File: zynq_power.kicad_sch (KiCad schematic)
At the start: 1 part, among them U2 XC7Z020-2CLG400I

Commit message: sch-updated
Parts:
- added C2, C200, C204, C209, C221, C224, C230, C233, C234, C235, C248: 100u, Capacitor_SMD:C_1206_3216Metric, symbol Device:C
- added C201, C205, C210, C216, C220, C223, C229, C232, C236, C237, C246, C247, C3: 4u7, Capacitor_SMD:C_0402_1005Metric, symbol Device:C
- added C202, C203, C206, C207, C208, C211, C215, C217, C218, C219, C222, C225, C226, C227, C228, C231, C238, C239, C240, C241, C242, C243, C244, C245, C4: 470n, Capacitor_SMD:C_0402_1005Metric, symbol Device:C
- added C400: 100n, Capacitor_SMD:C_0402_1005Metric, symbol Device:C
- added C612, C613: 47n, Capacitor_SMD:C_0402_1005Metric, symbol Device:C
- added FB200: 120R, FB_0402, symbol Schematic-Lib-PhilsLab:FB_0402
- added R401, R402: 12K, Resistor_SMD:R_0402_1005Metric, symbol Device:R
- added U1: XC7Z020-2CLG400I, Package_BGA:Xilinx_CLG400, symbol 2024-11-30_12-42-37:XC7Z020-2CLG400I
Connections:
- net GND: now reaches U2.F10 (RSVDGND)
- net GND: now also U2.A18 (GND), U2.B11 (GND), U2.C14 (GND), U2.C4 (GND), U2.C9 (GND), U2.D17 (GND), U2.E10 (GND), U2.E20 (GND), U2.F3 (GND), U2.F7 (GND), U2.G10 (GND), U2.G12 (GND), U2.G16 (GND), U2.H11 (GND), U2.H13 (GND), U2.H19 (GND), U2.H7 (GND), U2.H9 (GND), U2.J10 (GNDADC_0), U2.J12 (GND), U2.J2 (GND), U2.J8 (GND), U2.K11 (GND), U2.K13 (GND), U2.K15 (GND), U2.K5 (GND), U2.K7 (GND), U2.L12 (GND), U2.L18 (GND), U2.L8 (GND), U2.M1 (GND), U2.M11 (GND), U2.M13 (GND), U2.M7 (GND), U2.N10 (GND), U2.N12 (GND), U2.N14 (GND), U2.N4 (GND), U2.N8 (GND), U2.P11 (GND), U2.P13 (GND), U2.P17 (GND), U2.P7 (GND), U2.P9 (GND), U2.R12 (GND), U2.R8 (GND), U2.T3 (GND), U2.T7 (GND), U2.U6 (GND), U2.V9 (GND), U2.W2 (GND), U2.Y5 (GND), C2.2, C200.2, C201.2, C202.2, C203.2, C204.2, C205.2, C206.2, C207.2, C208.2, C209.2, C210.2, C211.2, C215.2, C216.2, C217.2, C218.2, C219.2, C220.2, C221.2, C222.2, C223.2, C224.2, C225.2, C226.2, C227.2, C228.2, C229.2, C230.2, C231.2, C232.2, C233.2, C234.2, C235.2, C236.2, C237.2, C238.2, C239.2, C240.2, C241.2, C242.2, C243.2, C244.2, C245.2, C246.2, C247.2, C248.2, C3.2, C4.2, C612.2, C613.2, U1.A8 (GND), U1.B1 (GND), U1.K10 (VREFN_0), U1.L9 (VREFP_0)
- net at U2.R20 (GND): now also U2.T13 (GND), U2.U16 (GND), U2.V19 (GND), U2.W12 (GND), U2.Y15 (GND)
- net at U2.E11 (PS_MIO_VREF_501): now also C400.1, R401.2, R402.1
- net +1V8: now reaches U2.F11 (VCCBATT_0)
- net +1V8: now also U2.J11 (VCCAUX), U2.J9 (VCCADC_0), U2.L11 (VCCAUX), U2.N11 (VCCAUX), U2.N9 (VCCAUX), U2.P10 (VCCAUX), U2.R9 (VCCAUX), C2.1, C217.1, C218.1, C219.1, C220.1, C221.1, C222.1, C223.1, C224.1, C3.1, C4.1, FB200.2, R402.2, U1.A13 (VCCO_MIO1_501), U1.B16 (VCCO_MIO1_501), U1.D12 (VCCO_MIO1_501), U1.E15 (VCCO_MIO1_501), U1.F8 (VCCPAUX), U1.G9 (VCCPAUX), U1.H8 (VCCPAUX), U1.K8 (VCCPAUX), U1.M8 (VCCPAUX)
- net PL_B35_L6_N: now reaches U2.F17 (IO_L6N_T0_VREF_35)
- net +1V0: now reaches U2.G11 (VCCBRAM)
- net +1V0: now also U2.G13 (VCCINT), U2.H10 (VCCBRAM), U2.H12 (VCCINT), U2.J13 (VCCINT), U2.K12 (VCCINT), U2.L13 (VCCINT), U2.M12 (VCCINT), U2.N13 (VCCINT), U2.P12 (VCCINT), U2.R13 (VCCINT), C200.1, C201.1, C202.1, C203.1, C204.1, C205.1, C206.1, C207.1, C208.1, C231.1, C232.1, C233.1, U1.G7 (VCCPINT), U1.J7 (VCCPINT), U1.L7 (VCCPINT), U1.N7 (VCCPINT), U1.P8 (VCCPINT), U1.R7 (VCCPINT)
- net +0V675: now reaches U2.H6 (PS_DDR_VREF0_502)
- net +0V675: now also U2.P6 (PS_DDR_VREF1_502), C612.1, C613.1
- net +3V3: now reaches U2.K6 (VCCO_0)
- net +3V3: now also U2.N6 (RSVDVCC3), U2.R6 (RSVDVCC2), U2.T6 (RSVDVCC1), C209.1, C210.1, C211.1, C234.1, C235.1, C236.1, C237.1, C238.1, C239.1, C240.1, C241.1, C242.1, C243.1, C244.1, C245.1, C246.1, C247.1, C248.1, U1.B6 (VCCO_MIO0_500), U1.C19 (VCCO_35), U1.D7 (VCCO_MIO0_500), U1.F18 (VCCO_35), U1.H14 (VCCO_35), U1.J17 (VCCO_35), U1.K20 (VCCO_35), U1.M16 (VCCO_35), U1.N19 (VCCO_34), U1.R15 (VCCO_34), U1.T18 (VCCO_34), U1.T8 (VCCO_13), U1.U11 (VCCO_13), U1.V14 (VCCO_34), U1.W17 (VCCO_34), U1.W7 (VCCO_13), U1.Y10 (VCCO_13), U1.Y20 (VCCO_34)
- new net: C400.2, R401.1
- new net +1V35: C225.1, C226.1, C227.1, C228.1, C229.1, C230.1, U1.A3 (VCCO_DDR_502), U1.D2 (VCCO_DDR_502), U1.E5 (VCCO_DDR_502), U1.G1 (VCCO_DDR_502), U1.H4 (VCCO_DDR_502), U1.L3 (VCCO_DDR_502), U1.P2 (VCCO_DDR_502), U1.R5 (VCCO_DDR_502), U1.U1 (VCCO_DDR_502), U1.V4 (VCCO_DDR_502)
- new net +1V8_PLL: C215.1, C216.1, FB200.1, U1.G8 (VCCPLL)
- no-connect marks 0 -> 4
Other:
- note added: "GND Connection"
- note added: "POWER & ETC"
- moved on the sheet: U2E, U2G, U2H

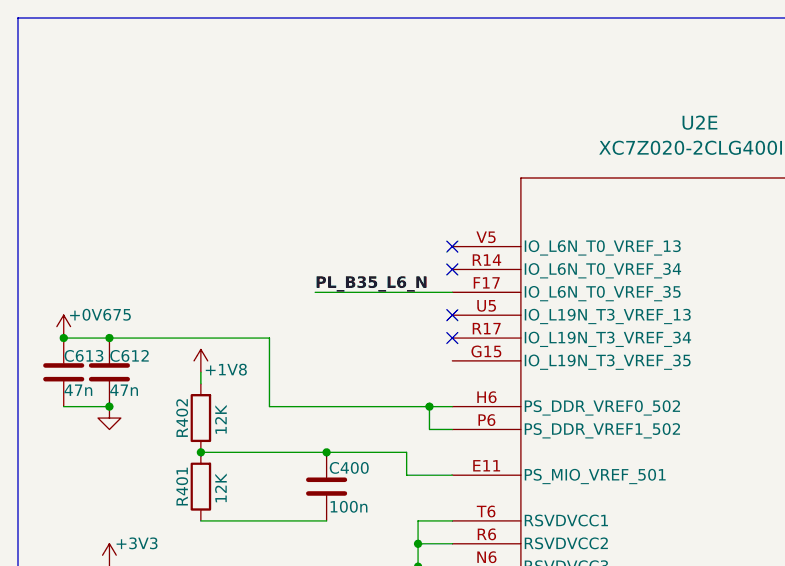
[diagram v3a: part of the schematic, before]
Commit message: sch updated zynq ddr
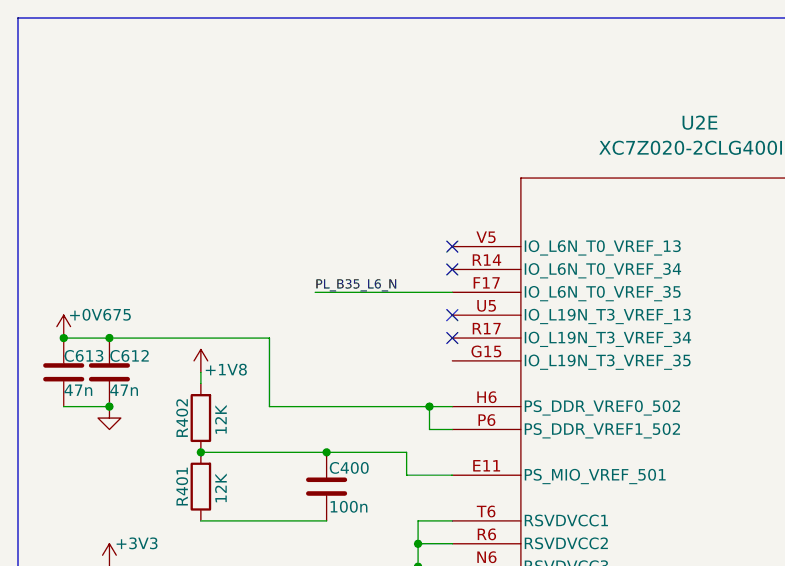
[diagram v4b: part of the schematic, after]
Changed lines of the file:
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@@
 		(effects
 			(font
-				(size 1.27 1.27)
-				(thickness 0.254)
-				(bold yes)
+				(size 1.016 1.016)
+				(thickness 0.127)
+				(color 82 86 255 1)
 			)
 			(justify left bottom)

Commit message: all page
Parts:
- removed C400: 100n, Capacitor_SMD:C_0402_1005Metric, symbol Device:C
- removed C612, C613: 47n, Capacitor_SMD:C_0402_1005Metric, symbol Device:C
- removed R401, R402: 12K, Resistor_SMD:R_0402_1005Metric, symbol Device:R
- removed U1, U2: XC7Z020-2CLG400I, Package_BGA:Xilinx_CLG400, symbol 2024-11-30_12-42-37:XC7Z020-2CLG400I
- added U6: XC7Z020-2CLG400I, zynq_sc7z0x0:CLG400, symbol Zynq_xc7z0x0-x:CMP-0363-00007-3
- renumbered C2 to C212, C3 to C213, C4 to C214
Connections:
- net +1V0: now also U6.G11 (VCCBRAM), U6.G13 (VCCINT), U6.G7 (VCCPINT), U6.H10 (VCCBRAM), U6.H12 (VCCINT), U6.J13 (VCCINT), U6.J7 (VCCPINT), U6.K12 (VCCINT), U6.L13 (VCCINT), U6.L7 (VCCPINT), U6.M12 (VCCINT), U6.N13 (VCCINT), U6.N7 (VCCPINT), U6.P12 (VCCINT), U6.P8 (VCCPINT), U6.R13 (VCCINT), U6.R7 (VCCPINT)
- net +1V35: now also U6.A3 (VCCO_DDR_502), U6.D2 (VCCO_DDR_502), U6.E5 (VCCO_DDR_502), U6.G1 (VCCO_DDR_502), U6.H4 (VCCO_DDR_502), U6.L3 (VCCO_DDR_502), U6.P2 (VCCO_DDR_502), U6.R5 (VCCO_DDR_502), U6.U1 (VCCO_DDR_502), U6.V4 (VCCO_DDR_502)
- net +1V8: now also U6.A13 (VCCO_MIO1_501), U6.B16 (VCCO_MIO1_501), U6.D12 (VCCO_MIO1_501), U6.E15 (VCCO_MIO1_501), U6.F11 (VCCBATT_0), U6.F8 (VCCPAUX), U6.G9 (VCCPAUX), U6.H8 (VCCPAUX), U6.J11 (VCCAUX), U6.J9 (VCCADC_0), U6.K8 (VCCPAUX), U6.L11 (VCCAUX), U6.M8 (VCCPAUX), U6.N11 (VCCAUX), U6.N9 (VCCAUX), U6.P10 (VCCAUX), U6.R9 (VCCAUX)
- net +1V8_PLL: now also U6.G8 (VCCPLL)
- net +3V3: now also U6.B6 (VCCO_MIO0_500), U6.C19 (VCCO_35), U6.D7 (VCCO_MIO0_500), U6.F18 (VCCO_35), U6.H14 (VCCO_35), U6.J17 (VCCO_35), U6.K20 (VCCO_35), U6.K6 (VCCO_0), U6.M16 (VCCO_35), U6.N19 (VCCO_34), U6.N6 (RSVDVCC3), U6.R15 (VCCO_34), U6.R6 (RSVDVCC2), U6.T18 (VCCO_34), U6.T6 (RSVDVCC1), U6.T8 (VCCO_13), U6.U11 (VCCO_13), U6.V14 (VCCO_34), U6.W17 (VCCO_34), U6.W7 (VCCO_13), U6.Y10 (VCCO_13), U6.Y20 (VCCO_34)
- net GND: now also U6.A18 (GND), U6.A8 (GND), U6.B1 (GND), U6.B11 (GND), U6.C14 (GND), U6.C4 (GND), U6.C9 (GND), U6.D17 (GND), U6.E10 (GND), U6.E20 (GND), U6.F10 (RSVDGND), U6.F3 (GND), U6.F7 (GND), U6.G10 (GND), U6.G12 (GND), U6.G16 (GND), U6.H11 (GND), U6.H13 (GND), U6.H19 (GND), U6.H7 (GND), U6.H9 (GND), U6.J10 (GNDADC_0), U6.J12 (GND), U6.J2 (GND), U6.J8 (GND), U6.K11 (GND), U6.K13 (GND), U6.K15 (GND), U6.K5 (GND), U6.K7 (GND), U6.L12 (GND), U6.L18 (GND), U6.L8 (GND), U6.M1 (GND), U6.M11 (GND), U6.M13 (GND), U6.M7 (GND), U6.N10 (GND), U6.N12 (GND), U6.N14 (GND), U6.N4 (GND), U6.N8 (GND), U6.P11 (GND), U6.P13 (GND), U6.P17 (GND), U6.P7 (GND), U6.P9 (GND), U6.R12 (GND), U6.R20 (GND), U6.R8 (GND), U6.T13 (GND), U6.T3 (GND), U6.T7 (GND), U6.U16 (GND), U6.U6 (GND), U6.V19 (GND), U6.V9 (GND), U6.W12 (GND), U6.W2 (GND), U6.Y15 (GND), U6.Y5 (GND)
- no-connect marks 4 -> 25
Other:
- note added: "Bank Supplies (0, 34, 35)"
- note added: "GND Connections"
- note added: "Main Supplies (INT, AUX, DDR, MIO)"
- note added: "Unused Pins"
- note added: "Zynq Power and Decoupling"
- note removed: "GND Connection"
- note removed: "POWER & ETC"
- title: (none) -> Zynq Power and Decoupling
- moved on the sheet: C200, C201, C202, C203, C204, C205, C206, C207, C208, C209, C210, C211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

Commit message: sch-to-pcb
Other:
- moved on the sheet: FB200

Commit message: xc7z020-fanout
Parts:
- U6: footprint zynq_sc7z0x0:CLG400 -> Package_BGA:Xilinx_CLG400
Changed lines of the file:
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@@
 			)
 		)
-		(property "Footprint" "zynq_sc7z0x0:CLG400"
+		(property "Footprint" "Package_BGA:Xilinx_CLG400"
 			(at 218.44 179.07 0)
 			(effects
@@
 			)
 		)
-		(property "Footprint" "zynq_sc7z0x0:CLG400"
+		(property "Footprint" "Package_BGA:Xilinx_CLG400"
 			(at 68.58 170.18 0)
 			(effects
@@
 			)
 		)
-		(property "Footprint" "zynq_sc7z0x0:CLG400"
+		(property "Footprint" "Package_BGA:Xilinx_CLG400"
 			(at 60.96 54.61 0)
 			(effects
@@
 			)
 		)
-		(property "Footprint" "zynq_sc7z0x0:CLG400"
+		(property "Footprint" "Package_BGA:Xilinx_CLG400"
 			(at 240.03 77.47 0)
 			(effects

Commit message: ram-update
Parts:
- C202, C203, C206, C207, C208, C211, C214, C215, C217, C218, C219, C222, C225, C226, C227, C228, C231, C238, C239, C240, C241, C242, C243, C244, C245: footprint Capacitor_SMD:C_0402_1005Metric -> easyeda2kicad_foorprint:C0201; LCSC C47339 -> C76591; Manufacturer Part Number CL05A474KP5NNNC -> C0603X5R1A474MT00NE
- FB200: footprint FB_0402 -> Footprint-Lib-PhilsLab:FB_0402
